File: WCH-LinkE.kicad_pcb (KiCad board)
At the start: 2 copper layers, 38.1 x 17.8 mm, 35 parts, among them J2 Conn_02x05_Odd_Even, J3 USB_C_Receptacle_USB2.0_16P, SW1 SW_Push, SW2 SW_Push, U1 RT9080-33GJ5, U2 CH32V305FBP6, U3 CH217K, U4 CH217K, Y2 12M

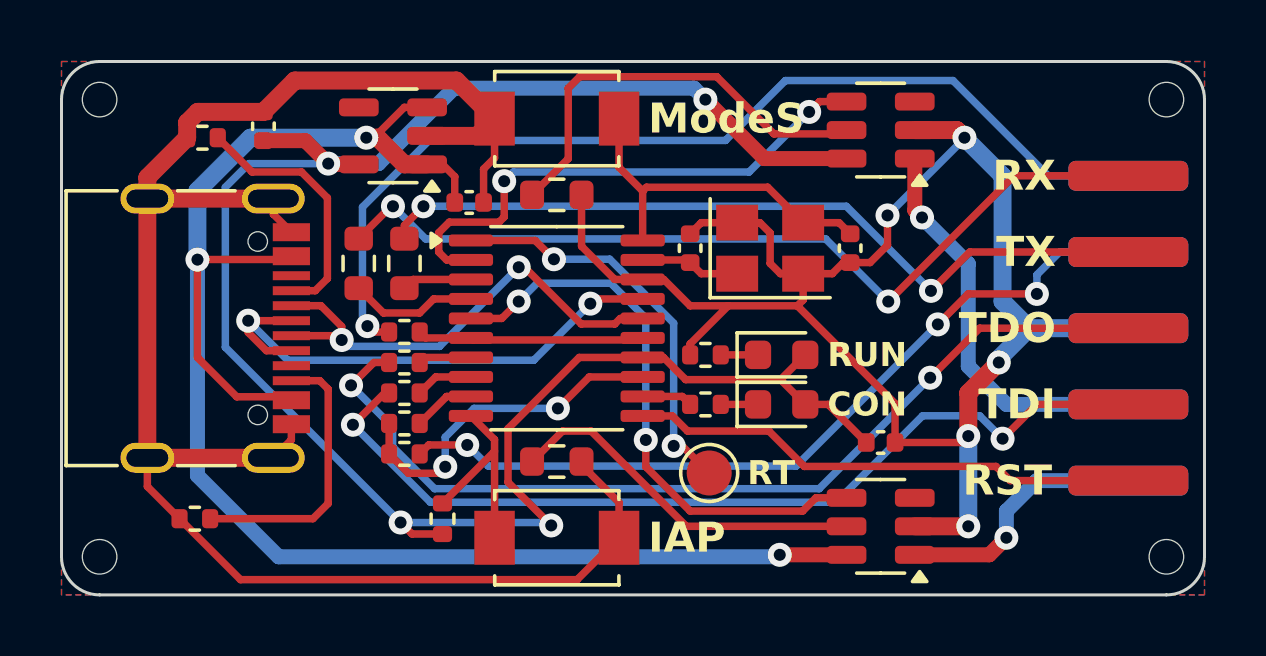
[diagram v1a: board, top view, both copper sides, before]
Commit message: fix library and fillzone
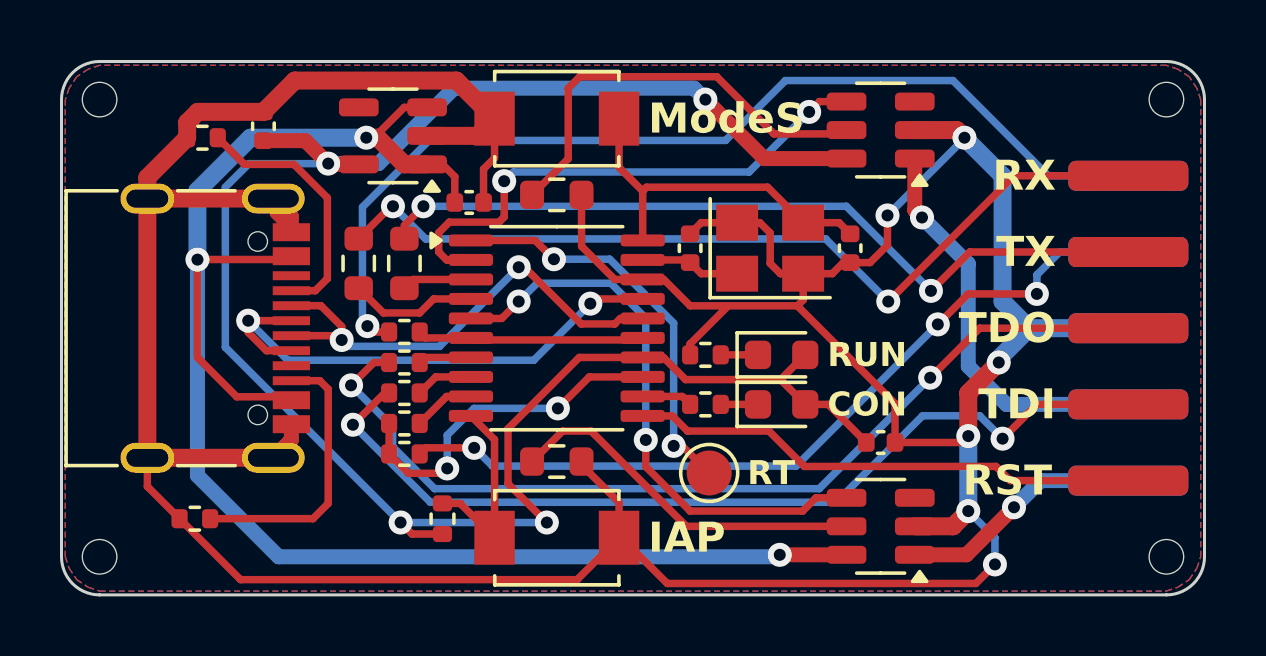
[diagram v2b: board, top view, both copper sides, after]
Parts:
- J3: value USB_C_Receptacle_USB2.0_16P -> USB_C_Receptacle_USB3.1_16P; footprint Connector_USB:USB_C_Receptacle_G-Switch_GT-USB-7010ASV -> USB:USB_C_Receptacle
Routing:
- net GND: track 117.4 -> 133.5 mm, vias 5 -> 6
- net /5V_OUT: track 8.66 -> 8.14 mm

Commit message: v1.1.0 pre-release
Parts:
- removed U1: RT9080-33GJ5, Package_TO_SOT_SMD:TSOT-23-5
- removed U3, U4: CH217K, Package_TO_SOT_SMD:SOT-23-6
- added C6: 0.1u, Capacitor_SMD:C_0402_1005Metric, F.Cu at (155.2, 116.7)
- added D3: 1N5819WS, Diode_SMD:D_SOD-323, F.Cu at (133.0, 113.0)
- added Q1: AO3401A, Package_TO_SOT_SMD:SOT-23, F.Cu at (154.9, 114.3)
- added Q2: AO3401A, Package_TO_SOT_SMD:SOT-23, F.Cu at (154.9, 124.5)
- added Q3: AO3401A, Package_TO_SOT_SMD:SOT-23, F.Cu at (138.0, 124.7)
- added U5: XC6206P332MR-G, Package_TO_SOT_SMD:SOT-23-3, F.Cu at (137.9, 113.8)
- C4: value 10u -> 1u
- C5: value 100n -> 0.1u
- J3: value USB_C_Receptacle_USB3.1_16P -> TYPE-C16PIN
- R13: value 150k -> 47k; footprint Resistor_SMD:R_0603_1608Metric -> Resistor_SMD:R_0402_1005Metric
- R14: value 300k -> 100k; footprint Resistor_SMD:R_0603_1608Metric -> Resistor_SMD:R_0402_1005Metric
- R8, R9: value 1k -> 5.1k
- moved R14 12.7 mm to (155.2, 118.7)
- moved R13 12.6 mm to (155.2, 117.7), turned to 180 degrees
- moved C4 7.31 mm to (140.6, 113.9), turned to -90 degrees
- moved C5 5.91 mm to (148.5, 123.0), turned to 180 degrees
- moved C2 5.41 mm to (135.3, 113.0), turned to -90 degrees
- moved TP1 3.53 mm to (151.4, 125.1)
- moved SW1 2.99 mm to (144.1, 114.0)
- moved H2 2.54 mm to (128.3, 113.0)
- moved H3 2.54 mm to (163.8, 113.0)
- moved C1 1.62 mm to (153.3, 117.1)
- moved R11 1.55 mm to (130.8, 113.0), turned to -90 degrees
- moved R12 1.45 mm to (132.6, 125.3), turned to 180 degrees
- moved C3 1.27 mm to (148.0, 116.7)
- moved J2 1.27 mm to (162.6, 119.4)
- moved J3 1.27 mm to (130.9, 119.4)
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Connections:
- C2 pad 1: +5V -> Net-(D3-K)
- R13 pad 1: Net-(U3-ISET) -> +5V
- R13 pad 2: GND -> Net-(Q2-G)
- R14 pad 1: Net-(U4-ISET) -> Net-(Q2-G)
- R14 pad 2: GND -> Net-(Q3-S)
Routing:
- net GND: track 133.5 -> 94.0 mm, vias 6 -> 3
- net Net-(Q3-S): track 0.00 -> 23.5 mm, vias 0 -> 2
- net Net-(U2-~{RST}): track 13.5 -> 33.8 mm
- net Net-(U4-ISET): track 14.7 -> 0.00 mm
- net +3V3: track 65.8 -> 51.3 mm
- net Net-(Q2-G): track 0.00 -> 12.3 mm
- net Net-(U3-ISET): track 12.2 -> 0.00 mm
- net +5V: track 55.6 -> 45.3 mm, vias 3 -> 2
- net /D_SWDIO: track 11.7 -> 21.5 mm, vias 2 -> 0
- net /PB12: track 19.2 -> 10.3 mm
- net /RST: track 17.1 -> 23.3 mm
- net /USB_N: track 16.3 -> 22.4 mm
- net /SWCLK/TCK: track 33.4 -> 28.3 mm
- net /D_SWCLK: track 7.57 -> 11.4 mm
- net Net-(U2-PB11): track 4.28 -> 7.78 mm, vias 0 -> 2
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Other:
- board size 38.1 x 17.8 mm -> 38.1 x 15.2 mm

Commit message: fix resistor value
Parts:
- J3: value TYPE-C16PIN -> USB_C_Receptacle_USB2.0_16P
- R13: value 47k -> 10k
- R14: value 100k -> 22k
